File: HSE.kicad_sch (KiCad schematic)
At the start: 4 parts, among them Y1 25MHz

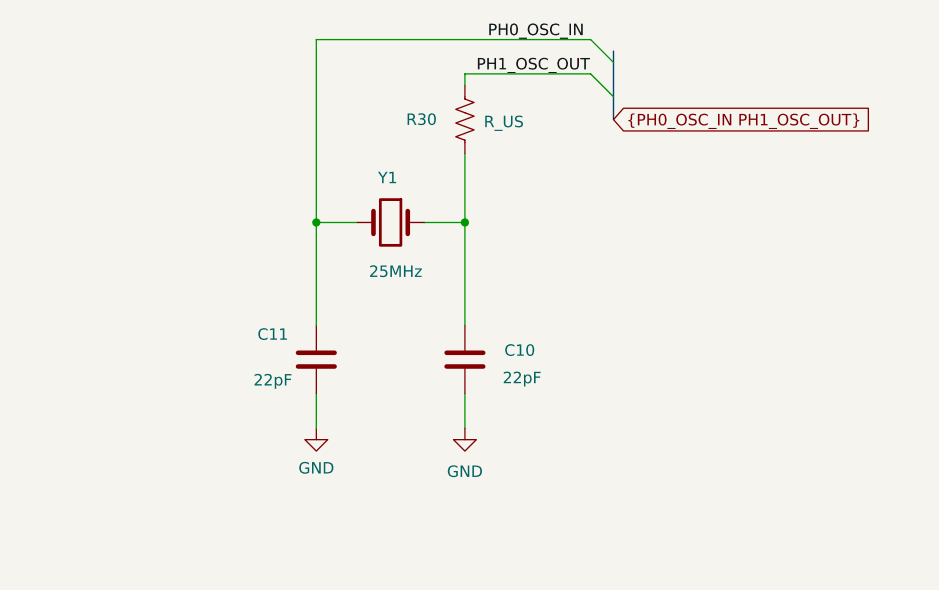
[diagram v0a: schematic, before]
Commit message: layout with F411 roughly good but needs work.
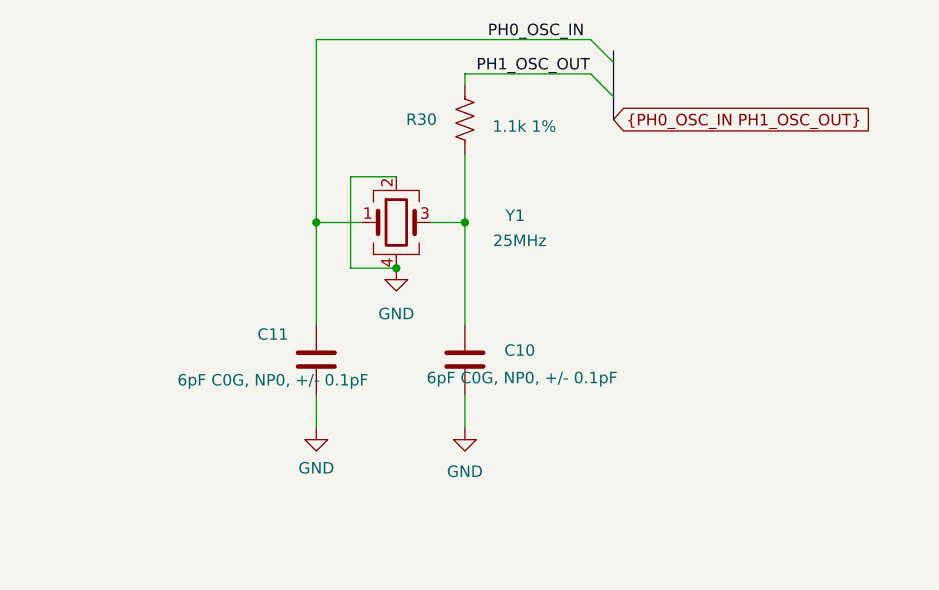
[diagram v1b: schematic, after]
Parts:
- removed Y1: 25MHz, symbol ProjectLib:Crystal
- added Y1: 25MHz, ProjectLib:Crystal_SMD_2016-4Pin_2.0x1.6mm, symbol ProjectLib:Crystal_GND24
- C10, C11: value 22pF -> 6pF C0G, NP0, +/- 0.1pF; footprint ProjectLib:C_0805_2012Metric -> ProjectLib:C_0603_1608Metric
- R30: value R_US -> 1.1k 1%; footprint (none) -> ProjectLib:R_0603_1608Metric
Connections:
- net GND: now also Y1.2, Y1.4
- net PH0_OSC_IN: now also Y1.1
- net at C10.2, R30.2: now also Y1.3
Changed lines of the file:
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@@
+		(color 0 0 0 0)
+	)
+	(junction
+		(at 147.32 99.06)
+		(diameter 0)
 		(color 0 0 0 0)
 	)
@@
 	(wire
 		(pts
-			(xy 150.495 93.98) (xy 154.94 93.98)
+			(xy 138.43 93.98) (xy 138.43 105.41)
+		)
+		(stroke
+			(width 0)
+			(type default)
+		)
+	)
+	(wire
+		(pts
+			(xy 154.94 93.98) (xy 154.94 105.41)
+		)
+		(stroke
+			(width 0)
+			(type default)
+		)
+	)
+	(wire
+		(pts
+			(xy 142.24 99.06) (xy 147.32 99.06)
 		)
 		(stroke
@@
 	(wire
 		(pts
-			(xy 138.43 105.41) (xy 138.43 93.98)
+			(xy 147.32 88.9) (xy 142.24 88.9)
+		)
+		(stroke
+			(width 0)
+			(type default)
+		)
+	)
+	(wire
+		(pts
+			(xy 138.43 93.98) (xy 143.51 93.98)
 		)
 		(stroke
@@
 	(wire
 		(pts
-			(xy 154.94 105.41) (xy 154.94 93.98)
-		)
-		(stroke
-			(width 0)
-			(type default)
-		)
-	)
-	(wire
-		(pts
 			(xy 154.94 77.47) (xy 154.94 78.74)
 		)
@@
 	(wire
 		(pts
-			(xy 138.43 93.98) (xy 142.875 93.98)
-		)
-		(stroke
-			(width 0)
-			(type default)
-		)
-	)
-	(wire
-		(pts
 			(xy 154.94 116.84) (xy 154.94 113.03)
 		)
@@
 		(pts
 			(xy 138.43 73.66) (xy 138.43 93.98)
+		)
+		(stroke
+			(width 0)
+			(type default)
+		)
+	)
+	(wire
+		(pts
+			(xy 142.24 88.9) (xy 142.24 99.06)
+		)
+		(stroke
+			(width 0)
+			(type default)
+		)
+	)
+	(wire
+		(pts
+			(xy 151.13 93.98) (xy 154.94 93.98)
 		)
 		(stroke
@@
 			)
 		)
-		(property "Value" "22pF"
+		(property "Value" "6pF C0G, NP0, +/- 0.1pF"
 			(at 161.29 111.252 0)
 			(effects
@@
 			)
 		)
-		(property "Footprint" "ProjectLib:C_0805_2012Metric"
+		(property "Footprint" "ProjectLib:C_0603_1608Metric"
 			(at 153.9748 105.41 0)
 			(effects
@@
 			)
 		)
-		(property "Value" "R_US"
-			(at 159.258 82.804 0)
-			(effects
-				(font
-					(size 1.27 1.27)
-				)
-			)
-		)
-		(property "Footprint" ""
+		(property "Value" "1.1k 1%"
+			(at 161.544 83.312 0)
+			(effects
+				(font
+					(size 1.27 1.27)
+				)
+			)
+		)
+		(property "Footprint" "ProjectLib:R_0603_1608Metric"
 			(at 155.956 82.804 90)
 			(effects
@@
 				(path "/0c2d0c14-8850-4a30-bb78-b2f40cb442ba/f12d0b95-be3f-41e2-8b41-943aec5e1edf/09b28461-e1e3-4809-8d37-797a691b7cc0"
 					(reference "R30")
-					(unit 1)
-				)
-			)
-		)
-	)
-	(symbol
-		(lib_id "ProjectLib:Crystal")
-		(at 146.685 93.98 0)
-		(mirror y)
-		(unit 1)
-		(exclude_from_sim no)
-		(in_bom yes)
-		(on_board yes)
-		(dnp no)
-		(property "Reference" "Y1"
-			(at 145.288 89.027 0)
-			(effects
-				(font
-					(size 1.27 1.27)
-				)
-				(justify right)
-			)
-		)
-		(property "Value" "25MHz"
-			(at 144.272 99.441 0)
-			(effects
-				(font
-					(size 1.27 1.27)
-				)
-				(justify right)
-			)
-		)
-		(property "Footprint" ""
-			(at 146.685 93.98 0)
-			(effects
-				(font
-					(size 1.27 1.27)
-				)
-				(hide yes)
-			)
-		)
-		(property "Datasheet" "~"
-			(at 146.685 93.98 0)
-			(effects
-				(font
-					(size 1.27 1.27)
-				)
-				(hide yes)
-			)
-		)
-		(property "Description" "crystal"
-			(at 146.685 93.98 0)
-			(effects
-				(font
-					(size 1.27 1.27)
-				)
-				(hide yes)
-			)
-		)
-		(property "MountType" "SMT"
-			(at 146.685 93.98 0)
-			(effects
-				(font
-					(size 1.27 1.27)
-				)
-				(hide yes)
-			)
-		)
-		(property "Notes" ""
-			(at 146.685 93.98 0)
-			(effects
-				(font
-					(size 1.27 1.27)
-				)
-				(hide yes)
-			)
-		)
-		(pin "2"
-		)
-		(pin "1"
-		)
-		(instances
-			(project "SensorProject_t16-pcb"
-				(path "/0c2d0c14-8850-4a30-bb78-b2f40cb442ba/f12d0b95-be3f-41e2-8b41-943aec5e1edf/09b28461-e1e3-4809-8d37-797a691b7cc0"
-					(reference "Y1")
 					(unit 1)
 				)
@@
 	)
 	(symbol
+		(lib_id "ProjectLib:Crystal_GND24")
+		(at 147.32 93.98 0)
+		(unit 1)
+		(exclude_from_sim no)
+		(in_bom yes)
+		(on_board yes)
+		(dnp no)
+		(property "Reference" "Y1"
+			(at 160.528 93.218 0)
+			(effects
+				(font
+					(size 1.27 1.27)
+				)
+			)
+		)
+		(property "Value" "25MHz"
+			(at 161.036 96.012 0)
+			(effects
+				(font
+					(size 1.27 1.27)
+				)
+			)
+		)
+		(property "Footprint" "ProjectLib:Crystal_SMD_2016-4Pin_2.0x1.6mm"
+			(at 147.32 93.98 0)
+			(effects
+				(font
+					(size 1.27 1.27)
+				)
+				(hide yes)
+			)
+		)
+		(property "Datasheet" "~"
+			(at 147.32 93.98 0)
+			(effects
+				(font
+					(size 1.27 1.27)
+				)
+				(hide yes)
+			)
+		)
+		(property "Description" "Four pin crystal, GND on pins 2 and 4"
+			(at 147.32 93.98 0)
+			(effects
+				(font
+					(size 1.27 1.27)
+				)
+				(hide yes)
+			)
+		)
+		(property "Manufacturer" ""
+			(at 147.32 93.98 0)
+			(effects
+				(font
+					(size 1.27 1.27)
+				)
+				(hide yes)
+			)
+		)
+		(property "Manuf Series" ""
+			(at 147.32 93.98 0)
+			(effects
+				(font
+					(size 1.27 1.27)
+				)
+				(hide yes)
+			)
+		)
+		(property "Manuf Part" ""
+			(at 147.32 93.98 0)
+			(effects
+				(font
+					(size 1.27 1.27)
+				)
+				(hide yes)
+			)
+		)
+		(pin "2"
+		)
+		(pin "3"
+		)
+		(pin "4"
+		)
+		(pin "1"
+		)
+		(instances
+			(project ""
+				(path "/0c2d0c14-8850-4a30-bb78-b2f40cb442ba/f12d0b95-be3f-41e2-8b41-943aec5e1edf/09b28461-e1e3-4809-8d37-797a691b7cc0"
+					(reference "Y1")
+					(unit 1)
+				)
+			)
+		)
+	)
+	(symbol
+		(lib_id "power:GND")
+		(at 147.32 99.06 0)
+		(unit 1)
+		(exclude_from_sim no)
+		(in_bom yes)
+		(on_board yes)
+		(dnp no)
+		(fields_autoplaced yes)
+		(property "Reference" "#PWR03"
+			(at 147.32 105.41 0)
+			(effects
+				(font
+					(size 1.27 1.27)
+				)
+				(hide yes)
+			)
+		)
+		(property "Value" "GND"
+			(at 147.32 104.14 0)
+			(effects
+				(font
+					(size 1.27 1.27)
+				)
+			)
+		)
+		(property "Footprint" ""
+			(at 147.32 99.06 0)
+			(effects
+				(font
+					(size 1.27 1.27)
+				)
+				(hide yes)
+			)
+		)
+		(property "Datasheet" ""
+			(at 147.32 99.06 0)
+			(effects
+				(font
+					(size 1.27 1.27)
+				)
+				(hide yes)
+			)
+		)
+		(property "Description" "Power symbol creates a global label with name \"GND\" , ground"
+			(at 147.32 99.06 0)
+			(effects
+				(font
+					(size 1.27 1.27)
+				)
+				(hide yes)
+			)
+		)
+		(pin "1"
+		)
+		(instances
+			(project ""
+				(path "/0c2d0c14-8850-4a30-bb78-b2f40cb442ba/f12d0b95-be3f-41e2-8b41-943aec5e1edf/09b28461-e1e3-4809-8d37-797a691b7cc0"
+					(reference "#PWR03")
+					(unit 1)
+				)
+			)
+		)
+	)
+	(symbol
 		(lib_id "power:GND")
 		(at 154.94 116.84 0)
@@
 			)
 		)
-		(property "Value" "22pF"
+		(property "Value" "6pF C0G, NP0, +/- 0.1pF"
 			(at 133.604 111.506 0)
 			(effects
@@
 			)
 		)
-		(property "Footprint" "ProjectLib:C_0805_2012Metric"
+		(property "Footprint" "ProjectLib:C_0603_1608Metric"
 			(at 137.4648 105.41 0)
 			(effects

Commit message: Most routing done but not checked. Moat around HSE but no net-tie yet.
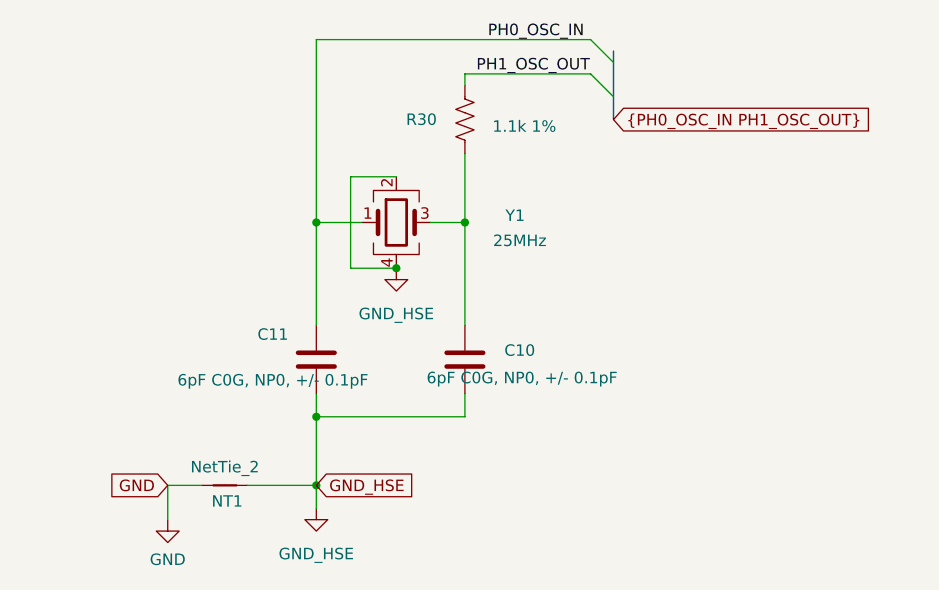
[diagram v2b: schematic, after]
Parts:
- added NT1: NetTie_2, symbol ProjectLib:NetTie_2
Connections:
- net GND: now also NT1.1; no longer C10.1, C11.1, Y1.2, Y1.4
- new net: Y1.2, Y1.4
- new net GND_HSE: C10.1, C11.1, NT1.2

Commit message: Moats complete. No errors. Net tie needs better zone and check crystals, BoM, etc. And general review.
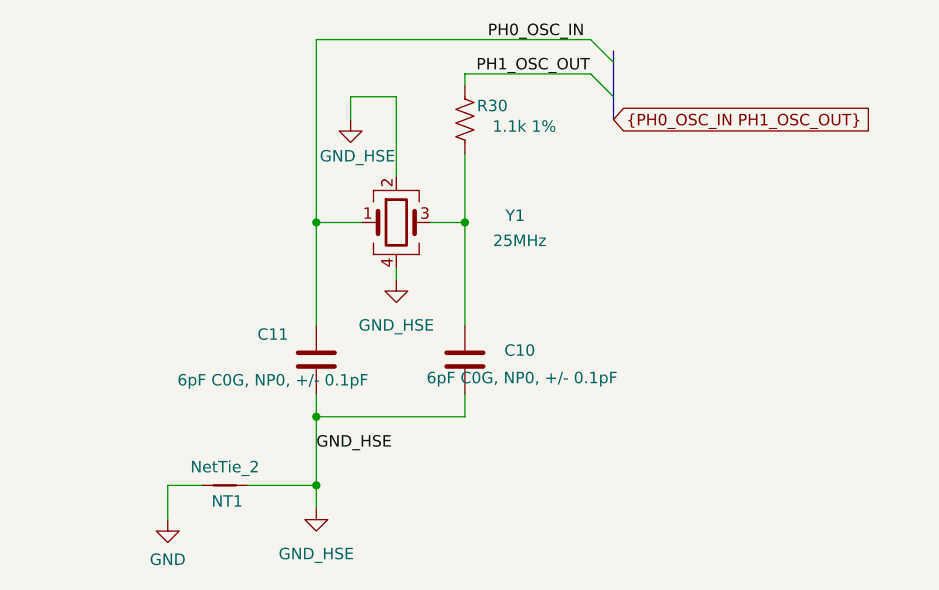
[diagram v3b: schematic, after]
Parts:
- NT1: footprint (none) -> ProjectLib:NetTie-2_SMD_Pad0.5mm
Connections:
- net GND_HSE: now also Y1.2, Y1.4
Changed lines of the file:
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@@
-		(color 0 0 0 0)
-	)
-	(junction
-		(at 147.32 99.06)
-		(diameter 0)
 		(color 0 0 0 0)
 	)
@@
 	(wire
 		(pts
-			(xy 142.24 99.06) (xy 147.32 99.06)
+			(xy 147.32 80.01) (xy 142.24 80.01)
 		)
 		(stroke
@@
 	(wire
 		(pts
-			(xy 147.32 88.9) (xy 142.24 88.9)
+			(xy 147.32 99.06) (xy 147.32 100.33)
 		)
 		(stroke
@@
 	(wire
 		(pts
-			(xy 142.24 88.9) (xy 142.24 99.06)
+			(xy 142.24 80.01) (xy 142.24 82.55)
 		)
 		(stroke
@@
 		(pts
 			(xy 138.43 115.57) (xy 138.43 113.03)
+		)
+		(stroke
+			(width 0)
+			(type default)
+		)
+	)
+	(wire
+		(pts
+			(xy 147.32 88.9) (xy 147.32 80.01)
 		)
 		(stroke
@@
 		)
 	)
-	(global_label "GND_HSE"
-		(shape input)
-		(at 138.43 123.19 0)
-		(fields_autoplaced yes)
+	(label "GND_HSE"
+		(at 138.43 119.38 0)
 		(effects
 			(font
 				(size 1.27 1.27)
 			)
-			(justify left)
-		)
-		(property "Intersheetrefs" "${INTERSHEET_REFS}"
-			(at 149.9423 123.19 0)
-			(effects
-				(font
-					(size 1.27 1.27)
-				)
-				(justify left)
-				(hide yes)
-			)
+			(justify left bottom)
 		)
 	)
@@
 		)
 	)
-	(global_label "GND"
-		(shape input)
-		(at 121.92 123.19 180)
-		(fields_autoplaced yes)
-		(effects
-			(font
-				(size 1.27 1.27)
-			)
-			(justify right)
-		)
-		(property "Intersheetrefs" "${INTERSHEET_REFS}"
-			(at 115.0643 123.19 0)
-			(effects
-				(font
-					(size 1.27 1.27)
-				)
-				(justify right)
-				(hide yes)
-			)
-		)
-	)
 	(symbol
 		(lib_id "ProjectLib:GND_HSE")
-		(at 147.32 99.06 0)
+		(at 147.32 100.33 0)
 		(unit 1)
 		(exclude_from_sim no)
@@
 		(fields_autoplaced yes)
 		(property "Reference" "#PWR03"
+			(at 147.32 106.68 0)
+			(effects
+				(font
+					(size 1.27 1.27)
+				)
+				(hide yes)
+			)
+		)
+		(property "Value" "GND_HSE"
 			(at 147.32 105.41 0)
 			(effects
@@
 					(size 1.27 1.27)
 				)
-				(hide yes)
-			)
-		)
-		(property "Value" "GND_HSE"
-			(at 147.32 104.14 0)
-			(effects
-				(font
-					(size 1.27 1.27)
-				)
 			)
 		)
 		(property "Footprint" ""
-			(at 147.32 99.06 0)
+			(at 147.32 100.33 0)
 			(effects
 				(font
@@
 		)
 		(property "Datasheet" ""
-			(at 147.32 99.06 0)
+			(at 147.32 100.33 0)
 			(effects
 				(font
@@
 		)
 		(property "Description" "Power symbol creates a global label with name \"GND_HSE\" , ground"
-			(at 147.32 99.06 0)
+			(at 147.32 100.33 0)
 			(effects
 				(font
@@
 				(path "/0c2d0c14-8850-4a30-bb78-b2f40cb442ba/f12d0b95-be3f-41e2-8b41-943aec5e1edf/09b28461-e1e3-4809-8d37-797a691b7cc0"
 					(reference "#PWR03")
+					(unit 1)
+				)
+			)
+		)
+	)
+	(symbol
+		(lib_id "ProjectLib:GND_HSE")
+		(at 142.24 82.55 0)
+		(unit 1)
+		(exclude_from_sim no)
+		(in_bom yes)
+		(on_board yes)
+		(dnp no)
+		(property "Reference" "#PWR061"
+			(at 142.24 88.9 0)
+			(effects
+				(font
+					(size 1.27 1.27)
+				)
+				(hide yes)
+			)
+		)
+		(property "Value" "GND_HSE"
+			(at 143.002 86.614 0)
+			(effects
+				(font
+					(size 1.27 1.27)
+				)
+			)
+		)
+		(property "Footprint" ""
+			(at 142.24 82.55 0)
+			(effects
+				(font
+					(size 1.27 1.27)
+				)
+				(hide yes)
+			)
+		)
+		(property "Datasheet" ""
+			(at 142.24 82.55 0)
+			(effects
+				(font
+					(size 1.27 1.27)
+				)
+				(hide yes)
+			)
+		)
+		(property "Description" "Power symbol creates a global label with name \"GND_HSE\" , ground"
+			(at 142.24 82.55 0)
+			(effects
+				(font
+					(size 1.27 1.27)
+				)
+				(hide yes)
+			)
+		)
+		(pin "1"
+		)
+		(instances
+			(project ""
+				(path "/0c2d0c14-8850-4a30-bb78-b2f40cb442ba/f12d0b95-be3f-41e2-8b41-943aec5e1edf/09b28461-e1e3-4809-8d37-797a691b7cc0"
+					(reference "#PWR061")
 					(unit 1)
 				)
@@
 		(dnp no)
 		(property "Reference" "R30"
-			(at 150.114 82.55 0)
+			(at 157.988 81.026 0)
 			(effects
 				(font
@@
 			)
 		)
-		(property "Footprint" ""
+		(property "Footprint" "ProjectLib:NetTie-2_SMD_Pad0.5mm"
 			(at 128.27 123.19 0)
 			(effects

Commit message: near complete, DRC good, ERC has a spurious error about ground on Y1.
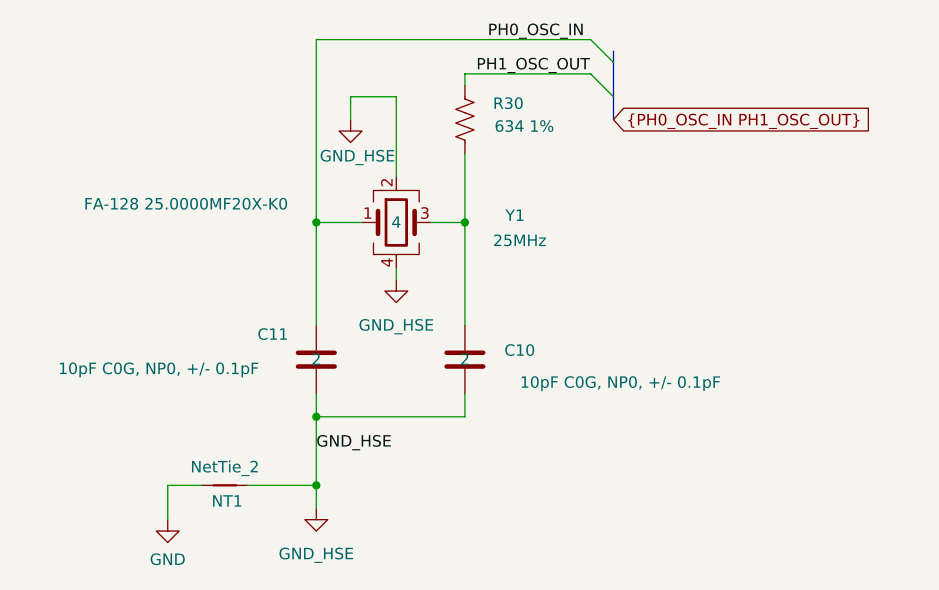
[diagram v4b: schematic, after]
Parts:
- C10, C11: value 6pF C0G, NP0, +/- 0.1pF -> 10pF C0G, NP0, +/- 0.1pF; pads (none) -> 2
- R30: value 1.1k 1% -> 634 1%; MountType (none) -> SMT; pads (none) -> 2
- Y1: Manufacturer (none) -> Epson; MfgPart (none) -> FA-128 25.0000MF20X-K0; MountType (none) -> SMT; pads (none) -> 4
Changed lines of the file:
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@@
 			)
 		)
-		(property "Value" "6pF C0G, NP0, +/- 0.1pF"
-			(at 161.29 111.252 0)
+		(property "Value" "10pF C0G, NP0, +/- 0.1pF"
+			(at 172.212 111.76 0)
 			(effects
 				(font
@@
 				)
 				(hide yes)
+			)
+		)
+		(property "pads" "2"
+			(at 154.94 109.22 0)
+			(effects
+				(font
+					(size 1.27 1.27)
+				)
 			)
 		)
@@
 		(dnp no)
 		(property "Reference" "R30"
-			(at 157.988 81.026 0)
-			(effects
-				(font
-					(size 1.27 1.27)
-				)
-			)
-		)
-		(property "Value" "1.1k 1%"
+			(at 159.766 80.772 0)
+			(effects
+				(font
+					(size 1.27 1.27)
+				)
+			)
+		)
+		(property "Value" "634  1%"
 			(at 161.544 83.312 0)
 			(effects
@@
 		)
 		(property "Description" "Resistor, US symbol"
+			(at 154.94 82.55 0)
+			(effects
+				(font
+					(size 1.27 1.27)
+				)
+				(hide yes)
+			)
+		)
+		(property "MountType" "SMT"
+			(at 154.94 82.55 0)
+			(effects
+				(font
+					(size 1.27 1.27)
+				)
+				(hide yes)
+			)
+		)
+		(property "pads" "2"
 			(at 154.94 82.55 0)
 			(effects
@@
 			)
 		)
-		(property "Datasheet" "~"
-			(at 147.32 93.98 0)
-			(effects
-				(font
-					(size 1.27 1.27)
-				)
-				(hide yes)
-			)
-		)
-		(property "Description" "Four pin crystal, GND on pins 2 and 4"
-			(at 147.32 93.98 0)
-			(effects
-				(font
-					(size 1.27 1.27)
-				)
-				(hide yes)
-			)
-		)
-		(property "Manufacturer" ""
+		(property "Datasheet" "https://support.epson.biz/td/api/doc_check.php?dl=brief_FA-128&lang=en"
+			(at 147.32 93.98 0)
+			(effects
+				(font
+					(size 1.27 1.27)
+				)
+				(hide yes)
+			)
+		)
+		(property "Description" "Four pin crystal.  10pF"
+			(at 147.32 93.98 0)
+			(effects
+				(font
+					(size 1.27 1.27)
+				)
+				(hide yes)
+			)
+		)
+		(property "Manufacturer" "Epson"
 			(at 147.32 93.98 0)
 			(effects
@@
 				)
 				(hide yes)
+			)
+		)
+		(property "MfgPart" "FA-128 25.0000MF20X-K0"
+			(at 123.952 91.948 0)
+			(effects
+				(font
+					(size 1.27 1.27)
+				)
+			)
+		)
+		(property "MountType" "SMT"
+			(at 147.32 93.98 0)
+			(effects
+				(font
+					(size 1.27 1.27)
+				)
+				(hide yes)
+			)
+		)
+		(property "pads" "4"
+			(at 147.32 93.98 0)
+			(effects
+				(font
+					(size 1.27 1.27)
+				)
 			)
 		)
@@
 			)
 		)
+		(property "pads" ""
+			(at 128.27 123.19 0)
+			(effects
+				(font
+					(size 1.27 1.27)
+				)
+			)
+		)
 		(pin "2"
 		)
@@
 			)
 		)
-		(property "Value" "6pF C0G, NP0, +/- 0.1pF"
-			(at 133.604 111.506 0)
+		(property "Value" "10pF C0G, NP0, +/- 0.1pF"
+			(at 120.904 110.236 0)
 			(effects
 				(font
@@
 			)
 		)
+		(property "pads" "2"
+			(at 138.43 109.22 0)
+			(effects
+				(font
+					(size 1.27 1.27)
+				)
+			)
+		)
